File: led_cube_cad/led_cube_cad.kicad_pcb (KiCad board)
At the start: 2 copper layers, 87 parts, among them U1 4099, U2 4099, U3 4099, U4 4099, U5 4099

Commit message: some routes
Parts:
- added RL0: 10k, Resistor_THT:R_Axial_DIN0309_L9.0mm_D3.2mm_P12.70mm_Horizontal, F.Cu at (224.0, 122.4)
- added RL1: 10k, Resistor_THT:R_Axial_DIN0309_L9.0mm_D3.2mm_P12.70mm_Horizontal, F.Cu at (213.4, 129.0)
- added RL2: 10k, Resistor_THT:R_Axial_DIN0309_L9.0mm_D3.2mm_P12.70mm_Horizontal, F.Cu at (203.7, 136.7)
- added RL3: 10k, Resistor_THT:R_Axial_DIN0309_L9.0mm_D3.2mm_P12.70mm_Horizontal, F.Cu at (195.1, 143.3)
- added RL4: 10k, Resistor_THT:R_Axial_DIN0309_L9.0mm_D3.2mm_P12.70mm_Horizontal, F.Cu at (186.4, 149.4)
- B0Q0, B0Q1, B0Q2, B0Q3, B0Q4, B1Q0, B1Q1, B1Q2, B1Q3, B1Q4, B2Q0, B2Q1, B2Q2, B2Q3, B2Q4, B3Q0, B3Q1, B3Q2, B3Q3, B3Q4, B4Q0, B4Q1, B4Q2, B4Q3, B4Q4: value BC636 -> BC560
- moved R46 145.5 mm to (126.2, 174.5), turned to 180 degrees
- moved NPN1 120.5 mm to (222.5, 97.5)
- moved R48 116.4 mm to (126.2, 161.5), turned to 180 degrees
- moved NPN3 112.0 mm to (202.2, 112.8)
- moved R41 108.7 mm to (126.2, 141.2), turned to 180 degrees
- moved R42 108.2 mm to (126.2, 134.6), turned to 180 degrees
- moved NPN5 108.0 mm to (187.5, 126.0), turned to 180 degrees
- moved R44 104.6 mm to (126.2, 121.9), turned to 180 degrees
- moved R47 104.5 mm to (126.2, 168.5), turned to 180 degrees
- moved NPN4 100.4 mm to (193.5, 119.9)
- moved R43 100.2 mm to (126.2, 128.3), turned to 180 degrees
- moved R50 97.5 mm to (126.2, 148.3), turned to 180 degrees
- moved R49 96.9 mm to (126.2, 154.9), turned to 180 degrees
- moved R24 96.2 mm to (79.8, 159.8)
- moved R25 96.2 mm to (79.8, 156.0)
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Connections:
- B0Q0 pad 1: +5V -> Net-(B0Q0-Pad1)
- B0Q0 pad 3: Net-(B0Q0-Pad3) -> +5V
- B0Q1 pad 1: +5V -> Net-(B0Q1-Pad1)
- B0Q1 pad 3: Net-(B0Q1-Pad3) -> +5V
- B0Q2 pad 1: +5V -> Net-(B0Q2-Pad1)
- B0Q2 pad 3: Net-(B0Q2-Pad3) -> +5V
- B0Q3 pad 1: +5V -> Net-(B0Q3-Pad1)
- B0Q3 pad 3: Net-(B0Q3-Pad3) -> +5V
- B0Q4 pad 1: +5V -> Net-(B0Q4-Pad1)
- B0Q4 pad 3: Net-(B0Q4-Pad3) -> +5V
- B1Q0 pad 1: +5V -> Net-(B1Q0-Pad1)
- B1Q0 pad 3: Net-(B1Q0-Pad3) -> +5V
- B1Q1 pad 1: +5V -> Net-(B1Q1-Pad1)
- B1Q1 pad 3: Net-(B1Q1-Pad3) -> +5V
- B1Q2 pad 1: +5V -> Net-(B1Q2-Pad1)
- B1Q2 pad 3: Net-(B1Q2-Pad3) -> +5V
- B1Q3 pad 1: +5V -> Net-(B1Q3-Pad1)
- B1Q3 pad 3: Net-(B1Q3-Pad3) -> +5V
- B1Q4 pad 1: +5V -> Net-(B1Q4-Pad1)
- B1Q4 pad 3: Net-(B1Q4-Pad3) -> +5V
- B2Q0 pad 1: +5V -> Net-(B2Q0-Pad1)
- B2Q0 pad 3: Net-(B2Q0-Pad3) -> +5V
- B2Q1 pad 1: +5V -> Net-(B2Q1-Pad1)
- B2Q1 pad 3: Net-(B2Q1-Pad3) -> +5V
- B2Q2 pad 1: +5V -> Net-(B2Q2-Pad1)
- B2Q2 pad 3: Net-(B2Q2-Pad3) -> +5V
- B2Q3 pad 1: +5V -> Net-(B2Q3-Pad1)
- B2Q3 pad 3: Net-(B2Q3-Pad3) -> +5V
- B2Q4 pad 1: +5V -> Net-(B2Q4-Pad1)
- B2Q4 pad 3: Net-(B2Q4-Pad3) -> +5V
- B3Q0 pad 1: +5V -> Net-(B3Q0-Pad1)
- B3Q0 pad 3: Net-(B3Q0-Pad3) -> +5V
- B3Q1 pad 1: +5V -> Net-(B3Q1-Pad1)
- B3Q1 pad 3: Net-(B3Q1-Pad3) -> +5V
- B3Q2 pad 1: +5V -> Net-(B3Q2-Pad1)
- B3Q2 pad 3: Net-(B3Q2-Pad3) -> +5V
- B3Q3 pad 1: +5V -> Net-(B3Q3-Pad1)
- B3Q3 pad 3: Net-(B3Q3-Pad3) -> +5V
- B3Q4 pad 1: +5V -> Net-(B3Q4-Pad1)
- B3Q4 pad 3: Net-(B3Q4-Pad3) -> +5V
- B4Q0 pad 1: +5V -> Net-(B4Q0-Pad1)
- B4Q0 pad 3: Net-(B4Q0-Pad3) -> +5V
- B4Q1 pad 1: +5V -> Net-(B4Q1-Pad1)
- B4Q1 pad 3: Net-(B4Q1-Pad3) -> +5V
- B4Q2 pad 1: +5V -> Net-(B4Q2-Pad1)
- B4Q2 pad 3: Net-(B4Q2-Pad3) -> +5V
- B4Q3 pad 1: +5V -> Net-(B4Q3-Pad1)
- B4Q3 pad 3: Net-(B4Q3-Pad3) -> +5V
- B4Q4 pad 1: +5V -> Net-(B4Q4-Pad1)
- B4Q4 pad 3: Net-(B4Q4-Pad3) -> +5V
- NPN1 pad 3: Net-(NPN1-Pad3) -> Net-(CubeConnector1-Pad22)
- NPN2 pad 3: Net-(NPN2-Pad3) -> Net-(CubeConnector1-Pad24)
- NPN3 pad 3: Net-(NPN3-Pad3) -> Net-(CubeConnector1-Pad26)
- NPN4 pad 3: Net-(NPN4-Pad3) -> Net-(CubeConnector1-Pad28)
- NPN5 pad 3: Net-(NPN5-Pad3) -> Net-(CubeConnector1-Pad30)
- R1 pad 2: Net-(B0Q0-Pad3) -> Net-(B0Q0-Pad2)
- R10 pad 2: Net-(B1Q4-Pad3) -> Net-(B1Q4-Pad2)
- R11 pad 2: Net-(B2Q0-Pad3) -> Net-(B2Q0-Pad2)
- R12 pad 2: Net-(B2Q1-Pad3) -> Net-(B2Q1-Pad2)
- R13 pad 2: Net-(B2Q2-Pad3) -> Net-(B2Q2-Pad2)
- R14 pad 2: Net-(B2Q3-Pad3) -> Net-(B2Q3-Pad2)
- R15 pad 2: Net-(B2Q4-Pad3) -> Net-(B2Q4-Pad2)
- R16 pad 2: Net-(B3Q0-Pad3) -> Net-(B3Q0-Pad2)
- R17 pad 2: Net-(B3Q1-Pad3) -> Net-(B3Q1-Pad2)
- R18 pad 2: Net-(B3Q2-Pad3) -> Net-(B3Q2-Pad2)
- R19 pad 2: Net-(B3Q3-Pad3) -> Net-(B3Q3-Pad2)
- R2 pad 2: Net-(B0Q1-Pad3) -> Net-(B0Q1-Pad2)
- R20 pad 2: Net-(B3Q4-Pad3) -> Net-(B3Q4-Pad2)
- R21 pad 2: Net-(B4Q0-Pad3) -> Net-(B4Q0-Pad2)
- R22 pad 2: Net-(B4Q1-Pad3) -> Net-(B4Q1-Pad2)
- R23 pad 2: Net-(B4Q2-Pad3) -> Net-(B4Q2-Pad2)
- R24 pad 2: Net-(B4Q3-Pad3) -> Net-(B4Q3-Pad2)
- R25 pad 2: Net-(B4Q4-Pad3) -> Net-(B4Q4-Pad2)
- R26 pad 2: Net-(B0Q0-Pad2) -> Net-(B0Q0-Pad1)
- R27 pad 2: Net-(B0Q1-Pad2) -> Net-(B0Q1-Pad1)
- R28 pad 2: Net-(B0Q2-Pad2) -> Net-(B0Q2-Pad1)
- R29 pad 2: Net-(B0Q3-Pad2) -> Net-(B0Q3-Pad1)
- R3 pad 2: Net-(B0Q2-Pad3) -> Net-(B0Q2-Pad2)
- R30 pad 2: Net-(B0Q4-Pad2) -> Net-(B0Q4-Pad1)
- R31 pad 2: Net-(B1Q0-Pad2) -> Net-(B1Q0-Pad1)
- R32 pad 2: Net-(B1Q1-Pad2) -> Net-(B1Q1-Pad1)
- R33 pad 2: Net-(B1Q2-Pad2) -> Net-(B1Q2-Pad1)
- R34 pad 2: Net-(B1Q3-Pad2) -> Net-(B1Q3-Pad1)
- R35 pad 2: Net-(B1Q4-Pad2) -> Net-(B1Q4-Pad1)
- R36 pad 2: Net-(B2Q0-Pad2) -> Net-(B2Q0-Pad1)
- R37 pad 2: Net-(B2Q1-Pad2) -> Net-(B2Q1-Pad1)
- R38 pad 2: Net-(B2Q2-Pad2) -> Net-(B2Q2-Pad1)
- R39 pad 2: Net-(B2Q3-Pad2) -> Net-(B2Q3-Pad1)
- R4 pad 2: Net-(B0Q3-Pad3) -> Net-(B0Q3-Pad2)
- R40 pad 2: Net-(B2Q4-Pad2) -> Net-(B2Q4-Pad1)
- R41 pad 2: Net-(B3Q0-Pad2) -> Net-(B3Q0-Pad1)
- R42 pad 2: Net-(B3Q1-Pad2) -> Net-(B3Q1-Pad1)
- R43 pad 2: Net-(B3Q2-Pad2) -> Net-(B3Q2-Pad1)
- R44 pad 2: Net-(B3Q3-Pad2) -> Net-(B3Q3-Pad1)
- R45 pad 2: Net-(B3Q4-Pad2) -> Net-(B3Q4-Pad1)
- R46 pad 2: Net-(B4Q0-Pad2) -> Net-(B4Q0-Pad1)
- R47 pad 2: Net-(B4Q1-Pad2) -> Net-(B4Q1-Pad1)
- R48 pad 2: Net-(B4Q2-Pad2) -> Net-(B4Q2-Pad1)
- R49 pad 2: Net-(B4Q3-Pad2) -> Net-(B4Q3-Pad1)
- R5 pad 2: Net-(B0Q4-Pad3) -> Net-(B0Q4-Pad2)
- R50 pad 2: Net-(B4Q4-Pad2) -> Net-(B4Q4-Pad1)
- R6 pad 2: Net-(B1Q0-Pad3) -> Net-(B1Q0-Pad2)
- R7 pad 2: Net-(B1Q1-Pad3) -> Net-(B1Q1-Pad2)
- R8 pad 2: Net-(B1Q2-Pad3) -> Net-(B1Q2-Pad2)
- R9 pad 2: Net-(B1Q3-Pad3) -> Net-(B1Q3-Pad2)
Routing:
- net +5V: track 0.00 -> 849.8 mm
- net Net-(CubeConnector1-Pad1): track 0.00 -> 81.5 mm
- net Net-(CubeConnector1-Pad3): track 0.00 -> 76.7 mm
- net Net-(CubeConnector1-Pad40): track 0.00 -> 72.0 mm
- net Net-(CubeConnector1-Pad5): track 0.00 -> 71.2 mm
- net Net-(CubeConnector1-Pad7): track 0.00 -> 66.7 mm
- net Net-(CubeConnector1-Pad9): track 0.00 -> 61.8 mm
- net Net-(CubeConnector1-Pad11): track 0.00 -> 54.0 mm
- net Net-(CubeConnector1-Pad13): track 0.00 -> 49.2 mm
- net Net-(CubeConnector1-Pad15): track 0.00 -> 45.1 mm
- net Net-(CubeConnector1-Pad39): track 0.00 -> 43.2 mm
- net Net-(CubeConnector1-Pad17): track 0.00 -> 42.0 mm
- net Net-(CubeConnector1-Pad37): track 0.00 -> 41.5 mm
- net Net-(CubeConnector1-Pad19): track 0.00 -> 40.2 mm
- net Net-(CubeConnector1-Pad35): track 0.00 -> 39.9 mm
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
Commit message: backup
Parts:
- moved NPN1 2.74 mm to (225.0, 98.6), turned to 180 degrees
- moved NPN4 2.59 mm to (196.1, 119.4), turned to 180 degrees
- moved NPN2 2.59 mm to (214.4, 105.7), turned to 180 degrees
- moved NPN3 2.59 mm to (204.7, 112.3), turned to 180 degrees
- moved NPN5 0.07 mm to (187.5, 126.0)
- moved RL0 0.07 mm to (224.0, 122.4)
- moved RL1 0.07 mm to (213.3, 129.0)
- moved RL2 0.07 mm to (203.6, 136.7)
- moved RL3 0.07 mm to (195.0, 143.3)
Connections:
- R46 pad 1: Net-(CubeConnector1-Pad40) -> Net-(CubeConnector1-Pad32)
- R47 pad 1: Net-(CubeConnector1-Pad38) -> Net-(CubeConnector1-Pad34)
- R49 pad 1: Net-(CubeConnector1-Pad34) -> Net-(CubeConnector1-Pad38)
- R50 pad 1: Net-(CubeConnector1-Pad32) -> Net-(CubeConnector1-Pad40)
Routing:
- net GND: track 0.00 -> 410.9 mm
- net Net-(BoardControl1-Pad13): track 0.00 -> 383.2 mm
- net Net-(BoardControl1-Pad14): track 0.00 -> 359.2 mm
- net Net-(BoardControl1-Pad15): track 0.00 -> 334.2 mm
- net Net-(BoardControl1-Pad16): track 0.00 -> 310.0 mm
- net Net-(BoardControl1-Pad17): track 0.00 -> 286.1 mm
- net Net-(BoardControl1-Pad12): track 0.00 -> 116.8 mm
- net Net-(CubeConnector1-Pad32): track 0.00 -> 90.3 mm
- net Net-(BoardControl1-Pad11): track 0.00 -> 85.2 mm
- net Net-(CubeConnector1-Pad34): track 0.00 -> 80.0 mm
- net Net-(CubeConnector1-Pad36): track 0.00 -> 69.6 mm
- net Net-(CubeConnector1-Pad22): track 0.00 -> 62.1 mm
- net Net-(CubeConnector1-Pad38): track 0.00 -> 60.0 mm
- net Net-(BoardControl1-Pad10): track 0.00 -> 59.3 mm
- net Net-(CubeConnector1-Pad24): track 0.00 -> 53.4 mm
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
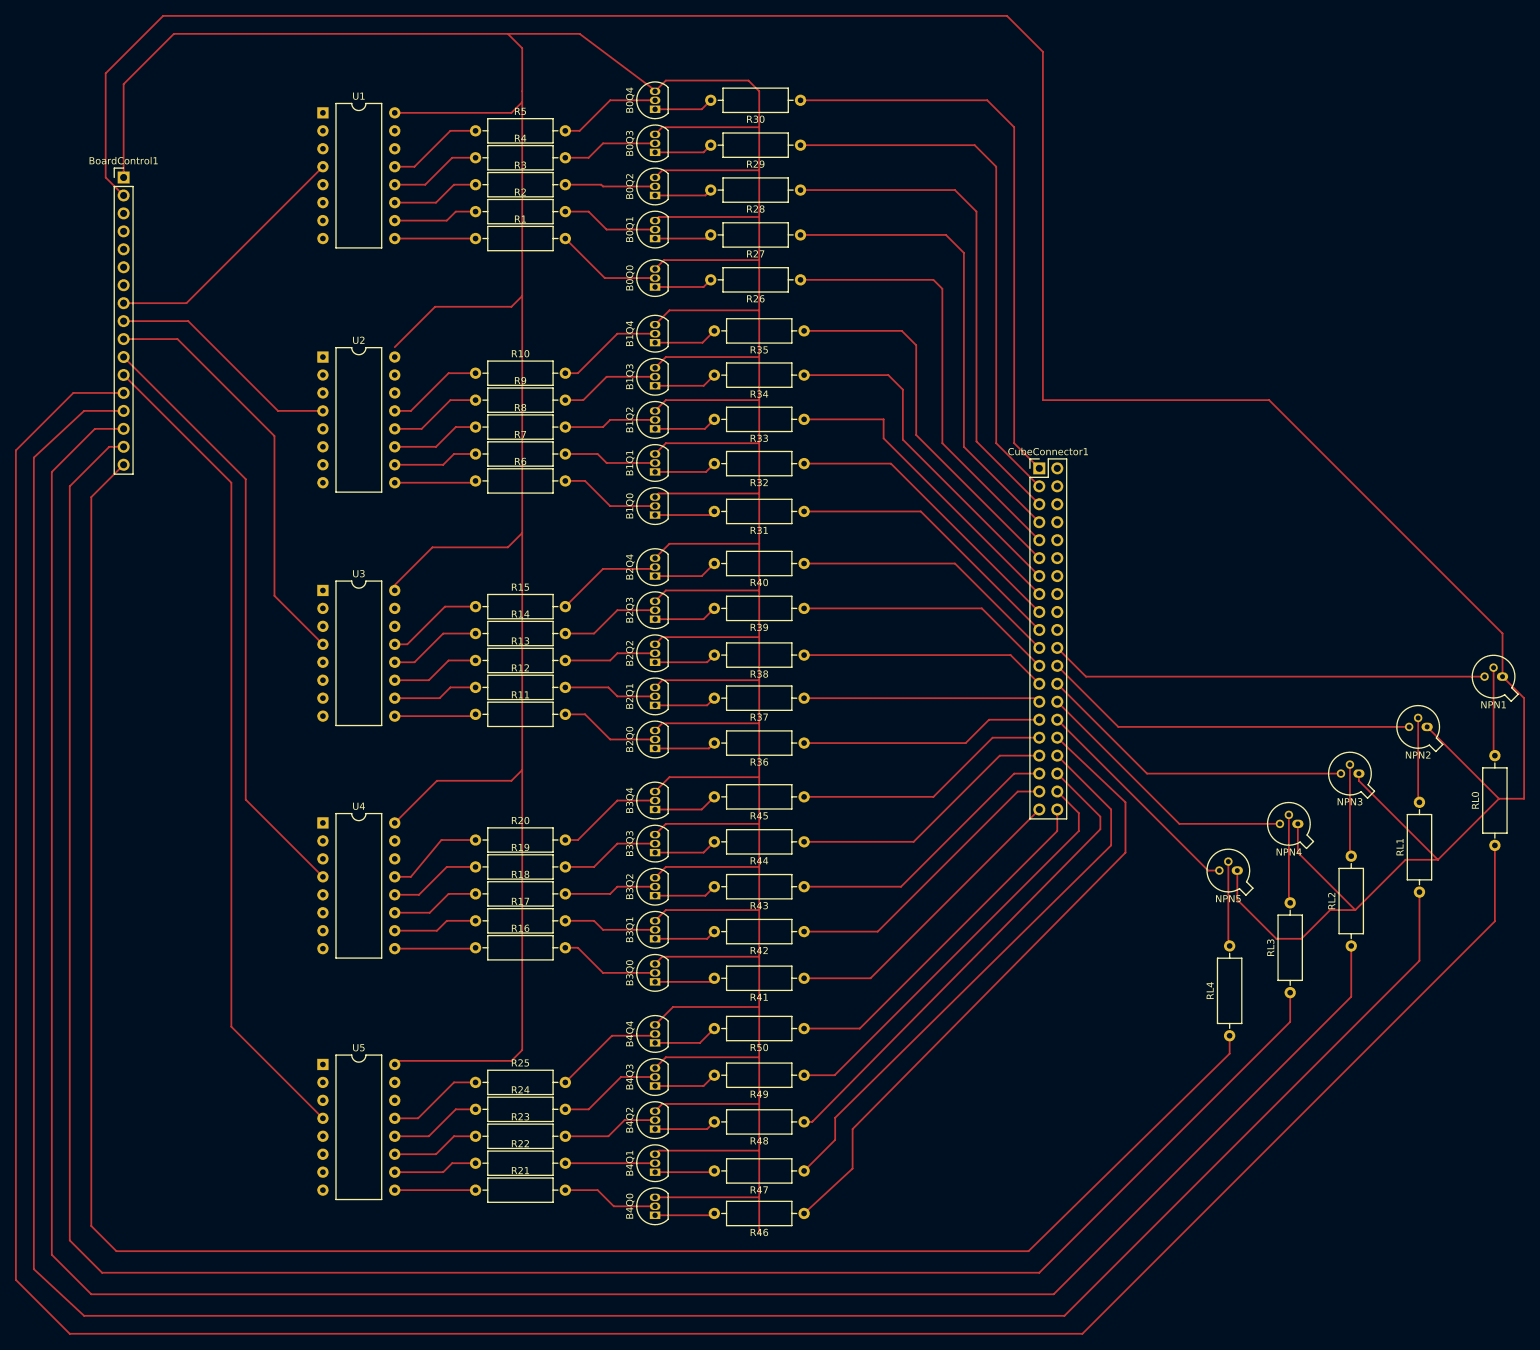
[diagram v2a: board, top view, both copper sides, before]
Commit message: track width
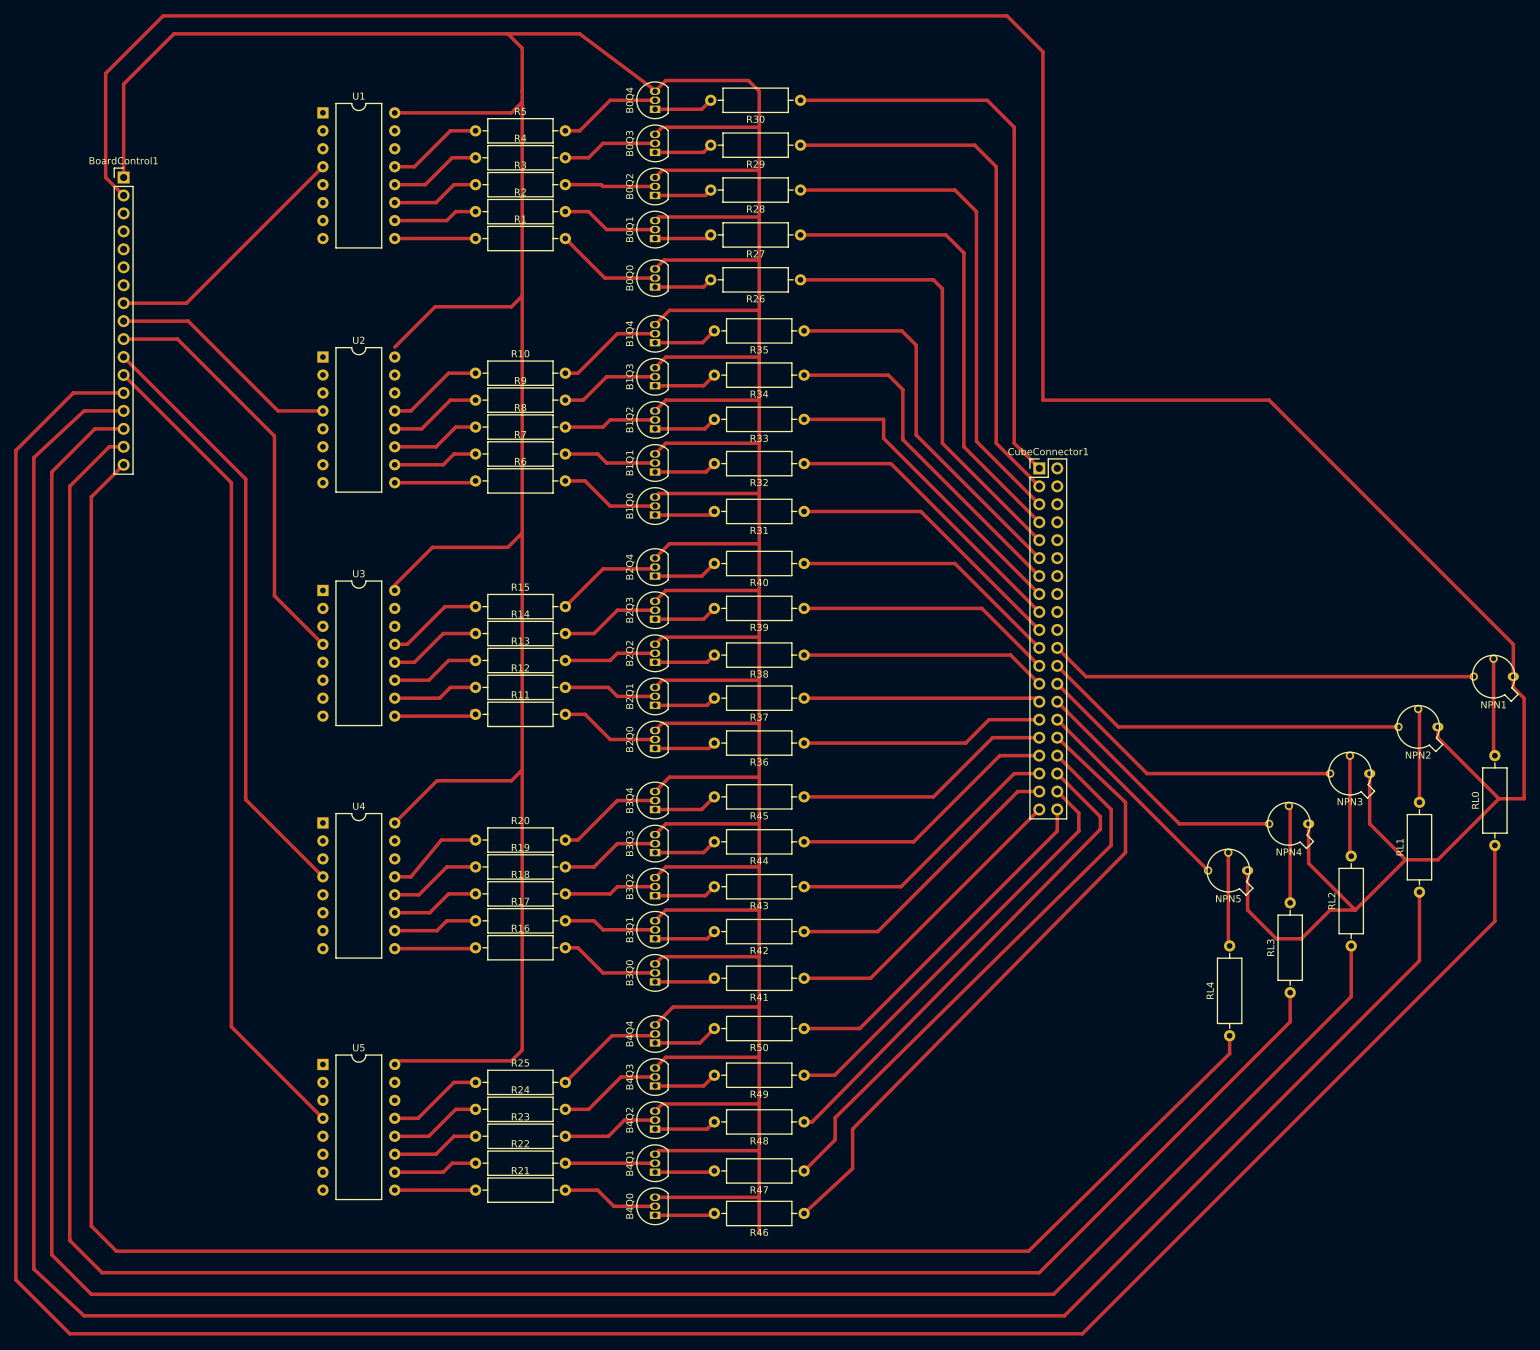
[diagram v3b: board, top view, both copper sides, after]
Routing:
- net GND: track 410.9 -> 406.5 mm
- net Net-(CubeConnector1-Pad30): track 31.8 -> 30.2 mm
- net Net-(NPN2-Pad2): track 12.0 -> 13.5 mm
- net Net-(NPN4-Pad2): track 12.5 -> 14.1 mm
- net Net-(CubeConnector1-Pad28): track 38.7 -> 37.1 mm
- net Net-(CubeConnector1-Pad26): track 45.4 -> 43.9 mm
- net Net-(CubeConnector1-Pad24): track 53.4 -> 51.8 mm
- net Net-(CubeConnector1-Pad22): track 62.1 -> 60.6 mm
- net Net-(NPN3-Pad2): track 13.0 -> 14.3 mm
- net Net-(NPN5-Pad2): track 12.0 -> 13.3 mm
- net Net-(NPN1-Pad2): track 12.5 -> 13.8 mm

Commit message: aligning thicks
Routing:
- net GND: track 406.5 -> 659.1 mm
- net +5V: track 883.1 -> 899.5 mm

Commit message: addressing wired
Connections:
- U1 pad 5: Net-(BoardControl1-Pad3) -> Net-(BoardControl1-Pad5)
- U1 pad 7: Net-(BoardControl1-Pad5) -> Net-(BoardControl1-Pad3)
- U2 pad 5: Net-(BoardControl1-Pad3) -> Net-(BoardControl1-Pad5)
- U2 pad 7: Net-(BoardControl1-Pad5) -> Net-(BoardControl1-Pad3)
- U3 pad 5: Net-(BoardControl1-Pad3) -> Net-(BoardControl1-Pad5)
- U3 pad 7: Net-(BoardControl1-Pad5) -> Net-(BoardControl1-Pad3)
- U4 pad 5: Net-(BoardControl1-Pad3) -> Net-(BoardControl1-Pad5)
- U4 pad 7: Net-(BoardControl1-Pad5) -> Net-(BoardControl1-Pad3)
- U5 pad 5: Net-(BoardControl1-Pad3) -> Net-(BoardControl1-Pad5)
- U5 pad 7: Net-(BoardControl1-Pad5) -> Net-(BoardControl1-Pad3)
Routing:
- net Net-(BoardControl1-Pad3): track 0.00 -> 269.3 mm
- net Net-(BoardControl1-Pad4): track 0.00 -> 257.8 mm
- net Net-(BoardControl1-Pad5): track 0.00 -> 246.3 mm
- net Net-(BoardControl1-Pad8): track 36.2 -> 41.9 mm
- net Net-(BoardControl1-Pad11): track 85.2 -> 85.8 mm

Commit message: tweaks
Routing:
- net Net-(BoardControl1-Pad12): track 116.6 -> 118.4 mm
- net GND: track 659.2 -> 660.1 mm
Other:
- net class Default: trace_width 0.25 -> 0.75
- rule trace_min: 0.2 -> 0.5
- board text added: "+ - A3 A2 A1 D R W1 W2 W3 W4 W5 L1 L2 L3 L4 L5"

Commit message: pads
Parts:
- added DATA1: Conn_01x01_Female, TestPoint:TestPoint_THTPad_D1.5mm_Drill0.7mm, F.Cu at (53.8, 23.9)
- added DATA2: Conn_01x01_Female, TestPoint:TestPoint_THTPad_D1.5mm_Drill0.7mm, F.Cu at (54.4, 58.4)
- added DATA3: Conn_01x01_Female, TestPoint:TestPoint_THTPad_D1.5mm_Drill0.7mm, F.Cu at (53.8, 91.4)
- added DATA4: Conn_01x01_Female, TestPoint:TestPoint_THTPad_D1.5mm_Drill0.7mm, F.Cu at (53.8, 124.5)
- added DATA5: Conn_01x01_Female, TestPoint:TestPoint_THTPad_D1.5mm_Drill0.7mm, F.Cu at (53.8, 158.5)
- added RESET1: Conn_01x01_Female, TestPoint:TestPoint_THTPad_D1.5mm_Drill0.7mm, F.Cu at (49.3, 21.3)
- added RESET2: Conn_01x01_Female, TestPoint:TestPoint_THTPad_D1.5mm_Drill0.7mm, F.Cu at (49.8, 55.9)
- added RESET3: Conn_01x01_Female, TestPoint:TestPoint_THTPad_D1.5mm_Drill0.7mm, F.Cu at (49.3, 88.9)
- added RESET4: Conn_01x01_Female, TestPoint:TestPoint_THTPad_D1.5mm_Drill0.7mm, F.Cu at (48.8, 121.9)
- added RESET5: Conn_01x01_Female, TestPoint:TestPoint_THTPad_D1.5mm_Drill0.7mm, F.Cu at (49.3, 156.0)
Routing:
- net Net-(BoardControl1-Pad7): track 0.00 -> 44.5 mm
- net Net-(BoardControl1-Pad6): track 0.00 -> 21.6 mm
- net Net-(BoardControl1-Pad12): track 118.4 -> 128.0 mm
- net Net-(BoardControl1-Pad11): track 85.8 -> 94.1 mm
- net Net-(BoardControl1-Pad10): track 59.3 -> 65.9 mm
- net Net-(BoardControl1-Pad8): track 41.9 -> 39.2 mm

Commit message: repositioned layer switches
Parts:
- moved RL4 59.1 mm to (131.6, 171.2)
- moved NPN5 55.4 mm to (139.7, 153.9)
- moved RL3 49.6 mm to (148.3, 160.0)
- moved NPN1 49.1 mm to (176.8, 89.4)
- moved NPN4 46.5 mm to (156.5, 143.8)
- moved RL0 43.7 mm to (181.9, 110.7)
- moved NPN2 40.7 mm to (173.7, 107.7)
- moved RL2 38.6 mm to (165.6, 143.3)
- moved RL1 36.5 mm to (176.8, 128.0)
- moved NPN3 36.2 mm to (170.7, 124.5)
- moved B0Q1 14.5 mm to (91.4, 32.0)
- moved B1Q1 14.5 mm to (91.4, 65.0)
- moved B1Q2 14.5 mm to (91.4, 58.9)
- moved B1Q3 14.5 mm to (91.4, 52.8)
- moved B1Q4 14.5 mm to (91.4, 46.7)
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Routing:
- net GND: track 660.1 -> 602.1 mm
- net Net-(BoardControl1-Pad17): track 286.1 -> 232.6 mm
- net Net-(BoardControl1-Pad16): track 310.0 -> 265.8 mm
- net Net-(CubeConnector1-Pad30): track 30.2 -> 68.8 mm
- net Net-(CubeConnector1-Pad22): track 60.6 -> 24.6 mm
- net Net-(BoardControl1-Pad15): track 334.2 -> 303.7 mm
- net Net-(CubeConnector1-Pad24): track 51.8 -> 27.6 mm
- net Net-(BoardControl1-Pad14): track 359.2 -> 337.3 mm
- net Net-(CubeConnector1-Pad28): track 37.1 -> 55.9 mm
- net Net-(BoardControl1-Pad13): track 383.2 -> 369.7 mm
- net Net-(CubeConnector1-Pad26): track 43.9 -> 37.0 mm
- net Net-(NPN3-Pad2): track 14.3 -> 10.1 mm
- net Net-(NPN4-Pad2): track 14.1 -> 11.3 mm
- net Net-(NPN2-Pad2): track 13.5 -> 11.9 mm
- net Net-(NPN5-Pad2): track 13.3 -> 12.0 mm
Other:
- board outline added: 238.8 x 208.3 mm
